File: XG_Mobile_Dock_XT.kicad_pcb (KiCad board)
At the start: 8 copper layers, 220.1 x 93 mm, 222 parts, among them IC1 PI2EQX22024XEAEX, J1 5-1775443-8, J10 SWD, J11 UART, J12 I2C1, J13 39301240, J14 I2C1, J2 20455-040E-76, J3 20455-040E-76, J5 USB_C_Receptacle, J6 455860005, J7 10147430-113T0LF, Q16 AO3401A, Q17 2N7002W, SW1 SW_Push, U1 DS320PR810NJXR, U12 STM32F030C8Tx, U2 DS320PR810NJXR

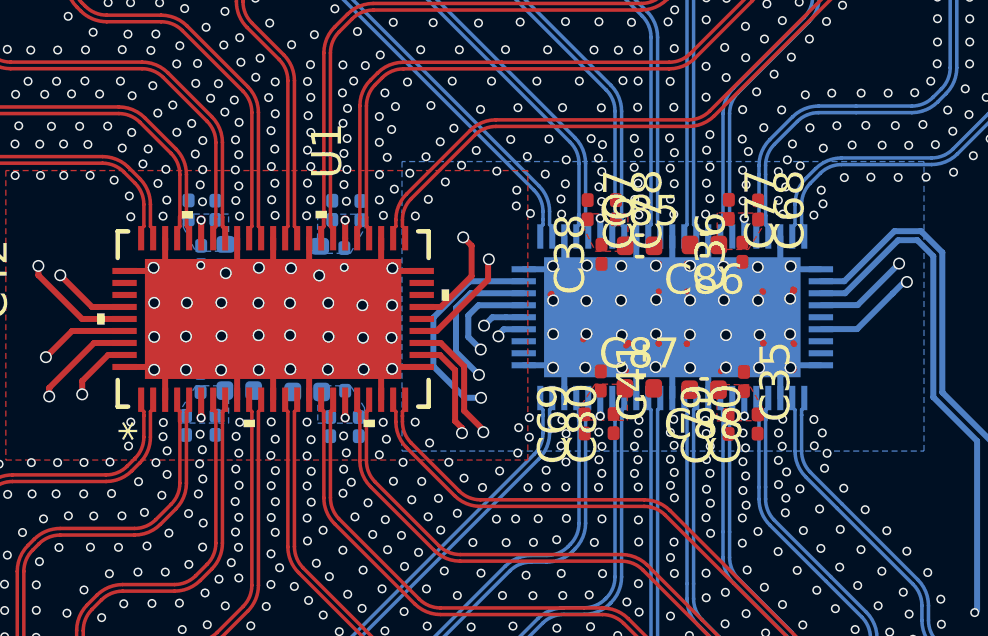
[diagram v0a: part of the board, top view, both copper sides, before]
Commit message: finished adding proper dedicated power layer to redrivers and lanes
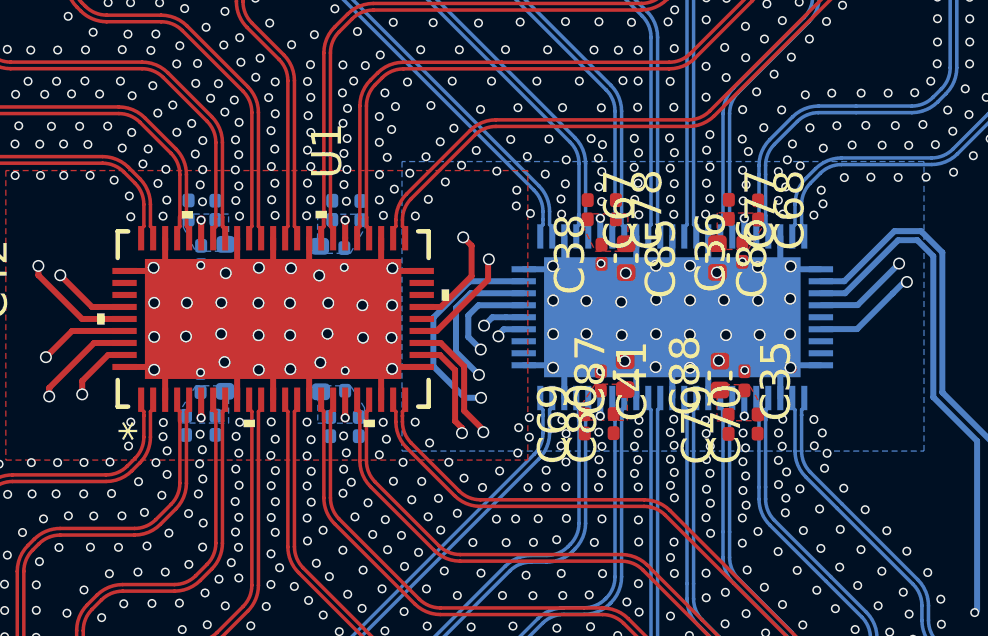
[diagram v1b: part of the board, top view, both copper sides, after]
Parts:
- moved C88 0.71 mm to (119.2, 88.1), turned to 90 degrees
- moved C84 0.67 mm to (105.9, 88.2), turned to 90 degrees
- moved C82 0.66 mm to (102.7, 88.2), turned to 90 degrees
- moved C87 0.64 mm to (116.0, 88.1), turned to 90 degrees
- moved C86 0.62 mm to (119.1, 84.2), turned to -90 degrees
- moved C85 0.61 mm to (116.0, 84.2), turned to -90 degrees
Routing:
- net Net-(U2-MODE): track 167.4 -> 171.6 mm
- net /Redriver/CPU_TO_GPU_EQ1_0: track 142.7 -> 139.1 mm
- net /Redriver/CPU_TO_GPU_EQ0_0: track 143.0 -> 146.5 mm
- net /Redriver/GPU_TO_CPU_EQ0_0: track 153.4 -> 155.2 mm
- net Net-(U2-GAIN0/SDA): track 175.6 -> 176.3 mm
- net /Redriver/CPU_TO_GPU_EQ0_1: track 112.6 -> 111.9 mm
- net GND: track 87.9 -> 87.3 mm, vias 2745 -> 2746
